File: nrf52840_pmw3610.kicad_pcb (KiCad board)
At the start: 2 copper layers, 18 x 33 mm, 3 parts, among them J1 PMW3360_Connector, J2 Battery_JST-PH, U1 SuperMini_nRF52840

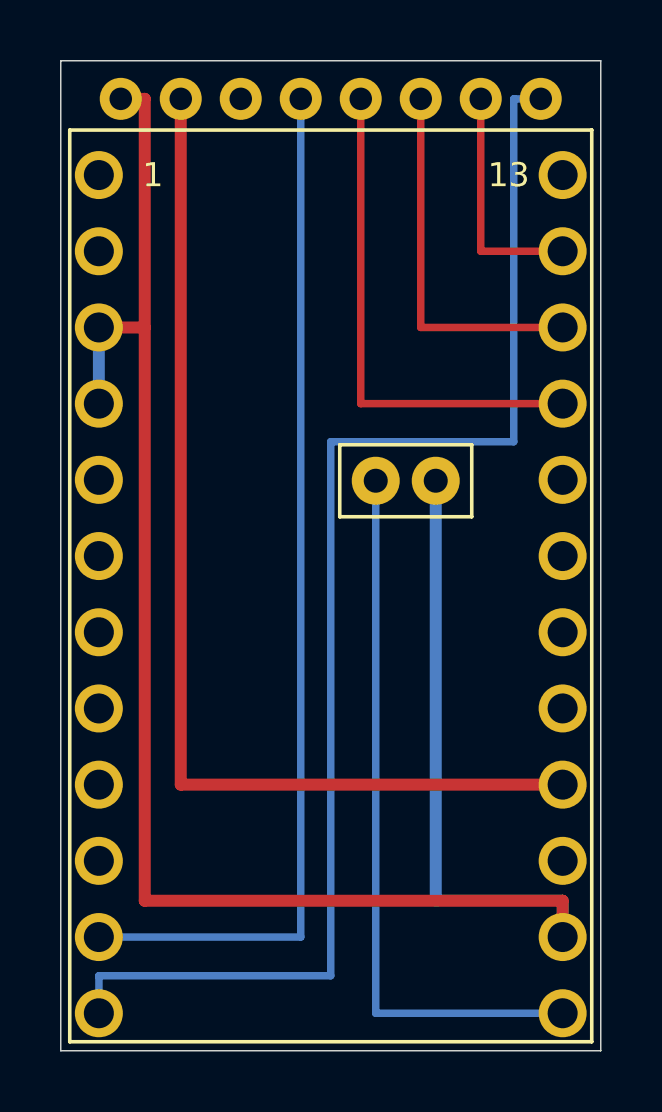
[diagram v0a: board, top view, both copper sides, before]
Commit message: fix: J2バッテリーコネクタをボード底部(y=31.0)に移動してnRF52840モジュールとの干渉を解消
Co-Authored-By: Claude Sonnet 4.6 <noreply@anthropic.com>
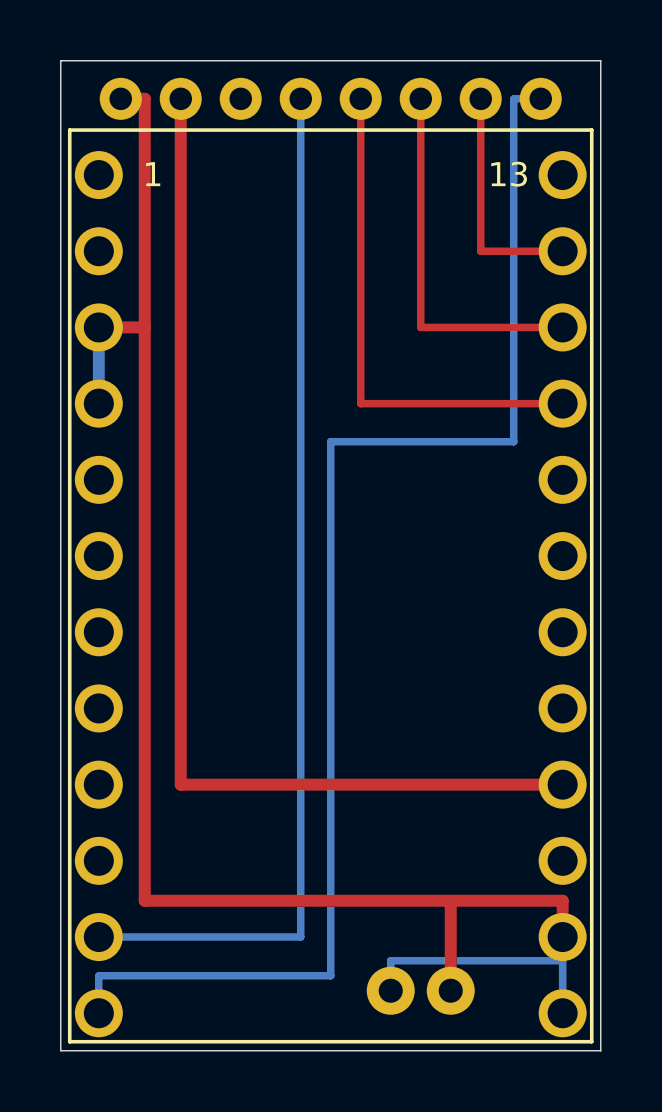
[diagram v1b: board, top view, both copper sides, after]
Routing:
- net GND: track 66.2 -> 49.7 mm
- net BATIN: track 24.0 -> 8.48 mm
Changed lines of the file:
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@@
 )
 (footprint "Connector_JST_PH_2pin" (layer "F.Cu") (at 135.0000 85.0000)
-  (fp_text reference "J2" (at 11.5000 12.0000) (layer "F.Fab")
+  (fp_text reference "J2" (at 12.0000 29.0000) (layer "F.Fab")
     (effects (font (size 0.8 0.8) (thickness 0.15))))
-  (fp_text value "Battery_JST-PH" (at 11.5000 16.0000) (layer "F.Fab")
+  (fp_text value "Battery_JST-PH" (at 12.0000 27.5000) (layer "F.Fab")
     (effects (font (size 0.8 0.8) (thickness 0.15))))
-    (pad "1" thru_hole oval (at 10.5000 14.0000) (size 1.6000 1.6000) (drill 0.8000) (layers "*.Cu" "*.Mask") (net 8 "BATIN"))
-    (pad "2" thru_hole circle (at 12.5000 14.0000) (size 1.6000 1.6000) (drill 0.8000) (layers "*.Cu" "*.Mask") (net 1 "GND"))
-  (fp_line (start 9.0500 12.5500) (end 13.9500 12.5500) (stroke (width 0.0500) (type default)) (layer "F.CrtYd"))
-  (fp_line (start 13.9500 12.5500) (end 13.9500 15.4500) (stroke (width 0.0500) (type default)) (layer "F.CrtYd"))
-  (fp_line (start 13.9500 15.4500) (end 9.0500 15.4500) (stroke (width 0.0500) (type default)) (layer "F.CrtYd"))
-  (fp_line (start 9.0500 15.4500) (end 9.0500 12.5500) (stroke (width 0.0500) (type default)) (layer "F.CrtYd"))
-  (fp_line (start 9.3000 12.8000) (end 13.7000 12.8000) (stroke (width 0.1200) (type default)) (layer "F.SilkS"))
-  (fp_line (start 13.7000 12.8000) (end 13.7000 15.2000) (stroke (width 0.1200) (type default)) (layer "F.SilkS"))
-  (fp_line (start 13.7000 15.2000) (end 9.3000 15.2000) (stroke (width 0.1200) (type default)) (layer "F.SilkS"))
-  (fp_line (start 9.3000 15.2000) (end 9.3000 12.8000) (stroke (width 0.1200) (type default)) (layer "F.SilkS"))
-  (fp_text user "B+" (at 10.5000 12.0000) (layer "F.Fab")
+    (pad "1" thru_hole oval (at 11.0000 31.0000) (size 1.6000 1.6000) (drill 0.8000) (layers "*.Cu" "*.Mask") (net 8 "BATIN"))
+    (pad "2" thru_hole circle (at 13.0000 31.0000) (size 1.6000 1.6000) (drill 0.8000) (layers "*.Cu" "*.Mask") (net 1 "GND"))
+  (fp_line (start 9.5500 29.5500) (end 14.4500 29.5500) (stroke (width 0.0500) (type default)) (layer "F.CrtYd"))
+  (fp_line (start 14.4500 29.5500) (end 14.4500 32.4500) (stroke (width 0.0500) (type default)) (layer "F.CrtYd"))
+  (fp_line (start 14.4500 32.4500) (end 9.5500 32.4500) (stroke (width 0.0500) (type default)) (layer "F.CrtYd"))
+  (fp_line (start 9.5500 32.4500) (end 9.5500 29.5500) (stroke (width 0.0500) (type default)) (layer "F.CrtYd"))
+  (fp_line (start 9.8000 29.8000) (end 14.2000 29.8000) (stroke (width 0.1200) (type default)) (layer "F.Fab"))
+  (fp_line (start 14.2000 29.8000) (end 14.2000 32.2000) (stroke (width 0.1200) (type default)) (layer "F.Fab"))
+  (fp_line (start 14.2000 32.2000) (end 9.8000 32.2000) (stroke (width 0.1200) (type default)) (layer "F.Fab"))
+  (fp_line (start 9.8000 32.2000) (end 9.8000 29.8000) (stroke (width 0.1200) (type default)) (layer "F.Fab"))
+  (fp_text user "B+" (at 11.0000 29.0000) (layer "F.Fab")
     (effects (font (size 0.8 0.8) (thickness 0.15))))
-  (fp_text user "B-" (at 12.5000 12.0000) (layer "F.Fab")
+  (fp_text user "B-" (at 13.0000 29.0000) (layer "F.Fab")
     (effects (font (size 0.8 0.8) (thickness 0.15))))
 )
@@
 (segment (start 139.0000 86.2700) (end 139.0000 109.1300) (width 0.4000) (layer "F.Cu") (net 2))
 (segment (start 139.0000 109.1300) (end 151.7300 109.1300) (width 0.4000) (layer "F.Cu") (net 2))
-(segment (start 145.5000 99.0000) (end 145.5000 116.7500) (width 0.2500) (layer "B.Cu") (net 8))
-(segment (start 145.5000 116.7500) (end 151.7300 116.7500) (width 0.2500) (layer "B.Cu") (net 8))
+(segment (start 146.0000 116.0000) (end 146.0000 115.0000) (width 0.2500) (layer "B.Cu") (net 8))
+(segment (start 146.0000 115.0000) (end 151.7300 115.0000) (width 0.2500) (layer "B.Cu") (net 8))
+(segment (start 151.7300 115.0000) (end 151.7300 116.7500) (width 0.2500) (layer "B.Cu") (net 8))
 (segment (start 151.0000 86.2700) (end 150.1000 86.2700) (width 0.2500) (layer "B.Cu") (net 6))
 (segment (start 150.1000 86.2700) (end 150.1000 97.7000) (width 0.2500) (layer "B.Cu") (net 6))
@@
 (segment (start 137.8000 113.0000) (end 151.7300 113.0000) (width 0.4000) (layer "F.Cu") (net 1))
 (segment (start 151.7300 113.0000) (end 151.7300 114.2100) (width 0.4000) (layer "F.Cu") (net 1))
-(segment (start 147.5000 99.0000) (end 147.5000 113.0000) (width 0.4000) (layer "B.Cu") (net 1))
-(segment (start 147.5000 113.0000) (end 151.7300 113.0000) (width 0.4000) (layer "B.Cu") (net 1))
-(segment (start 151.7300 113.0000) (end 151.7300 114.2100) (width 0.4000) (layer "B.Cu") (net 1))
+(segment (start 148.0000 116.0000) (end 148.0000 113.0000) (width 0.4000) (layer "F.Cu") (net 1))
 (segment (start 136.2700 93.8900) (end 136.2700 96.4300) (width 0.4000) (layer "B.Cu") (net 1))
 (gr_text "nRF52840+PMW3610" (at 144.0000 116.5000 0) (layer "F.Fab")
